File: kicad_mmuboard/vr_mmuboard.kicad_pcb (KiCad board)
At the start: 2 copper layers, 59.4 x 32.9 mm, 3 parts, among them J1 Conn_01x02_Male, U1 ST_MMU_SOCKET, U2 ST_MMU_PHY

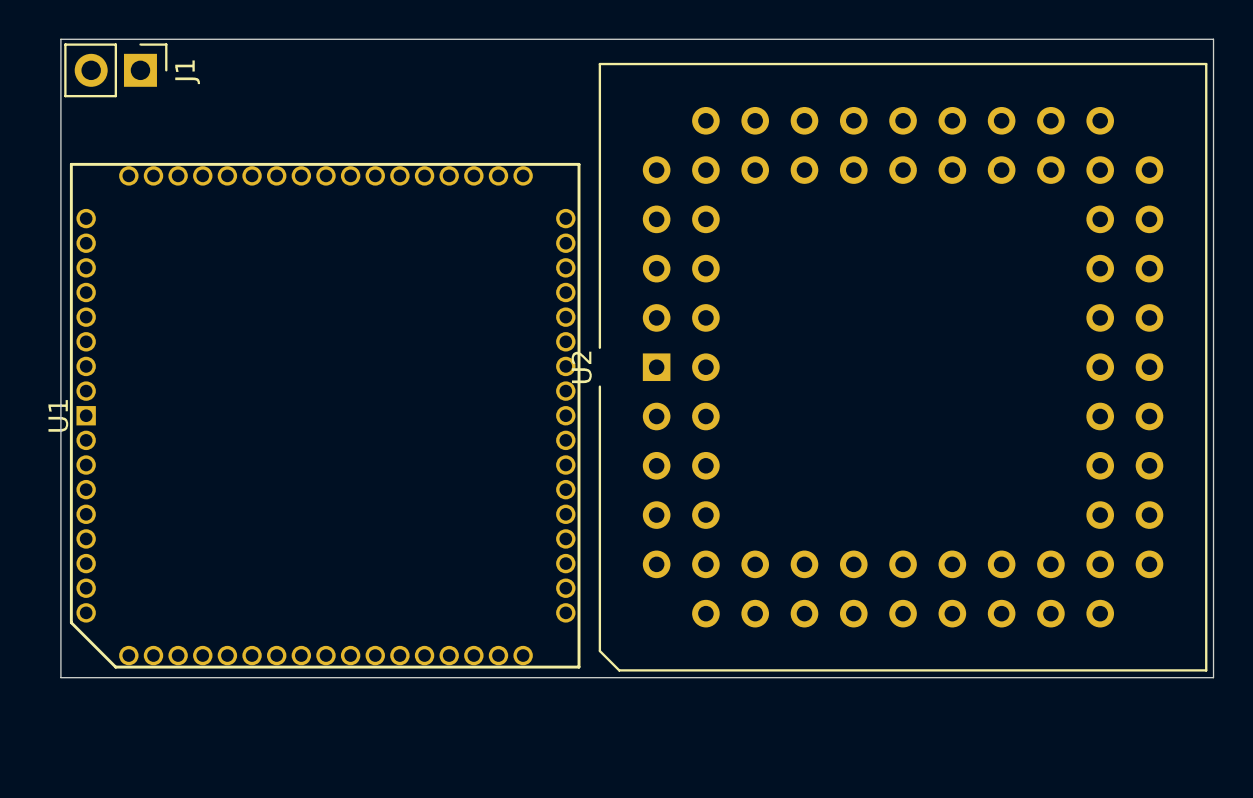
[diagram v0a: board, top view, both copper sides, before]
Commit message: MMUBoard added to repo
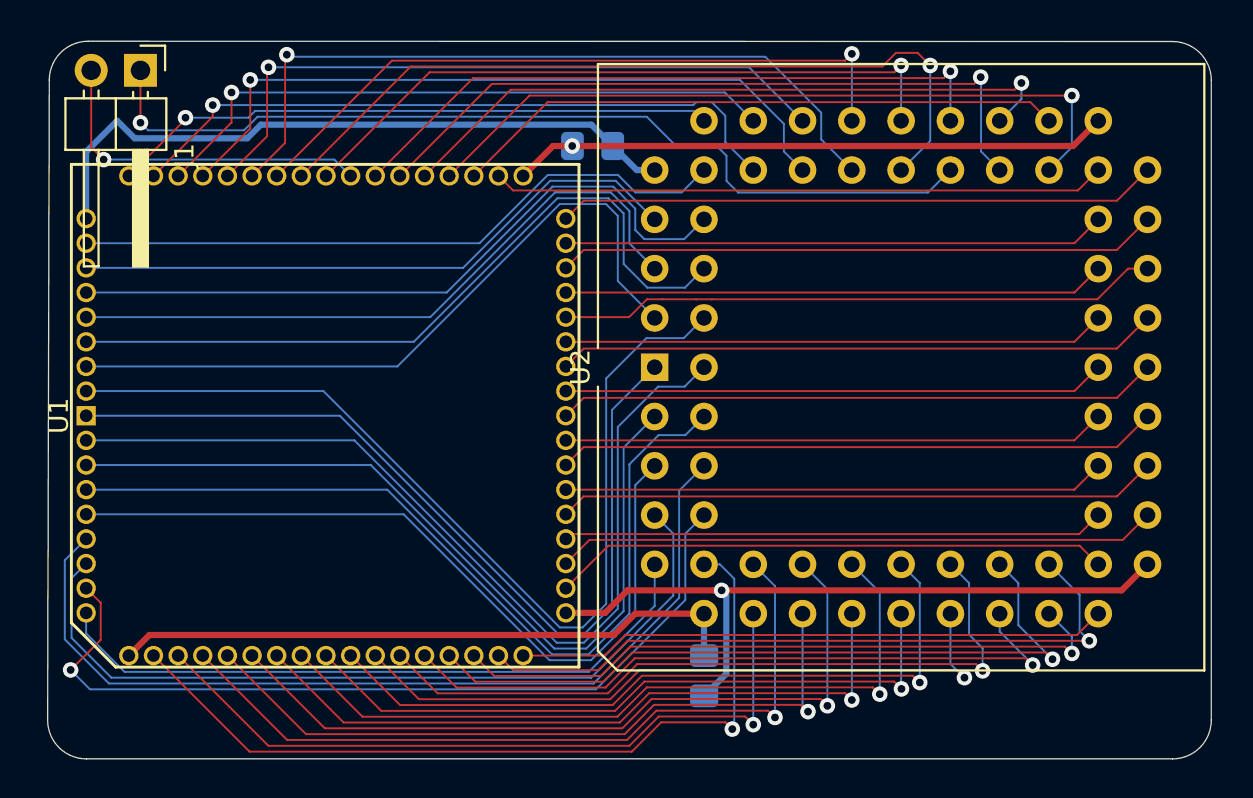
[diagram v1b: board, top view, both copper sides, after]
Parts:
- added C1: 1u, Capacitor_SMD:C_0805_2012Metric_Pad1.18x1.45mm_HandSolder, B.Cu at (160.2, 135.7)
- added C2: 1u, Capacitor_SMD:C_0805_2012Metric_Pad1.18x1.45mm_HandSolder, B.Cu at (154.5, 108.4)
- J1: footprint Connector_PinHeader_2.54mm:PinHeader_1x02_P2.54mm_Vertical -> Connector_PinHeader_2.54mm:PinHeader_1x02_P2.54mm_Horizontal
- moved U2 0.10 mm to (157.7, 119.8)
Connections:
- net Net-(U1-Pad10) renamed /VCC1
- net Net-(U1-Pad27) renamed /GND1
- net Net-(U1-Pad44) renamed /VCC2
- net Net-(U1-Pad61) renamed /GND2
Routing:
- net Net-(U1-Pad68): track 0.00 -> 50.3 mm
- net /VSYNC_MMU: track 0.00 -> 47.8 mm, vias 0 -> 1
- net Net-(U1-Pad2): track 0.00 -> 47.5 mm
- net Net-(U1-Pad6): track 0.00 -> 47.4 mm
- net Net-(U1-Pad1): track 0.00 -> 45.7 mm
- net Net-(U1-Pad4): track 0.00 -> 44.9 mm
- net Net-(U1-Pad8): track 0.00 -> 43.9 mm, vias 0 -> 1
- net Net-(U1-Pad3): track 0.00 -> 43.1 mm
- net Net-(U1-Pad11): track 0.00 -> 42.3 mm, vias 0 -> 1
- net Net-(U1-Pad7): track 0.00 -> 42.3 mm
- net Net-(U1-Pad53): track 0.00 -> 41.3 mm, vias 0 -> 1
- net Net-(U1-Pad5): track 0.00 -> 40.5 mm
- net Net-(U1-Pad13): track 0.00 -> 40.4 mm, vias 0 -> 1
- net Net-(U1-Pad15): track 0.00 -> 39.8 mm, vias 0 -> 1
- net Net-(U1-Pad55): track 0.00 -> 39.4 mm, vias 0 -> 1
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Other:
- board size 59.4 x 32.9 mm -> 60 x 37 mm
